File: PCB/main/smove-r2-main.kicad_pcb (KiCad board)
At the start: 4 copper layers, 25 x 30 mm, 47 parts, among them J1 TYPE-C-31-M-12, J2 Battery wire pads 2.54mm, SW2 RESET, SW3 BOOT / USER, U1 ESP32-C3-MINI-1-N4, U2 ICM-20948, U3 PCA9306DCUR, U4 AP2112K-3.3TRG1, U5 AP2112K-1.8TRG1, U6 BQ24074RGTR, U8 USBLC6-2SC6, U9 PESD5V0S2BT,215

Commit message: Make sure it's printer friendly
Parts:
- C3: value 22uF / 10V -> 22uF / 25V

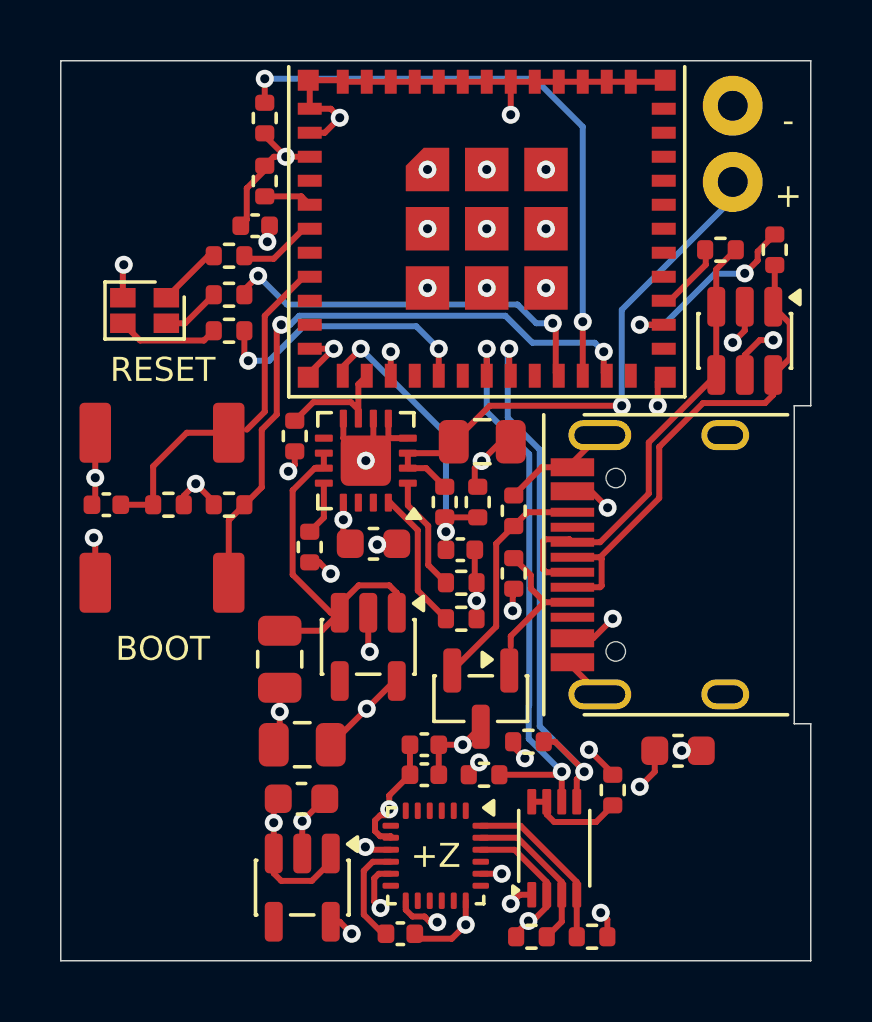
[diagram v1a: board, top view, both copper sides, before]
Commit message: Add mounting holes
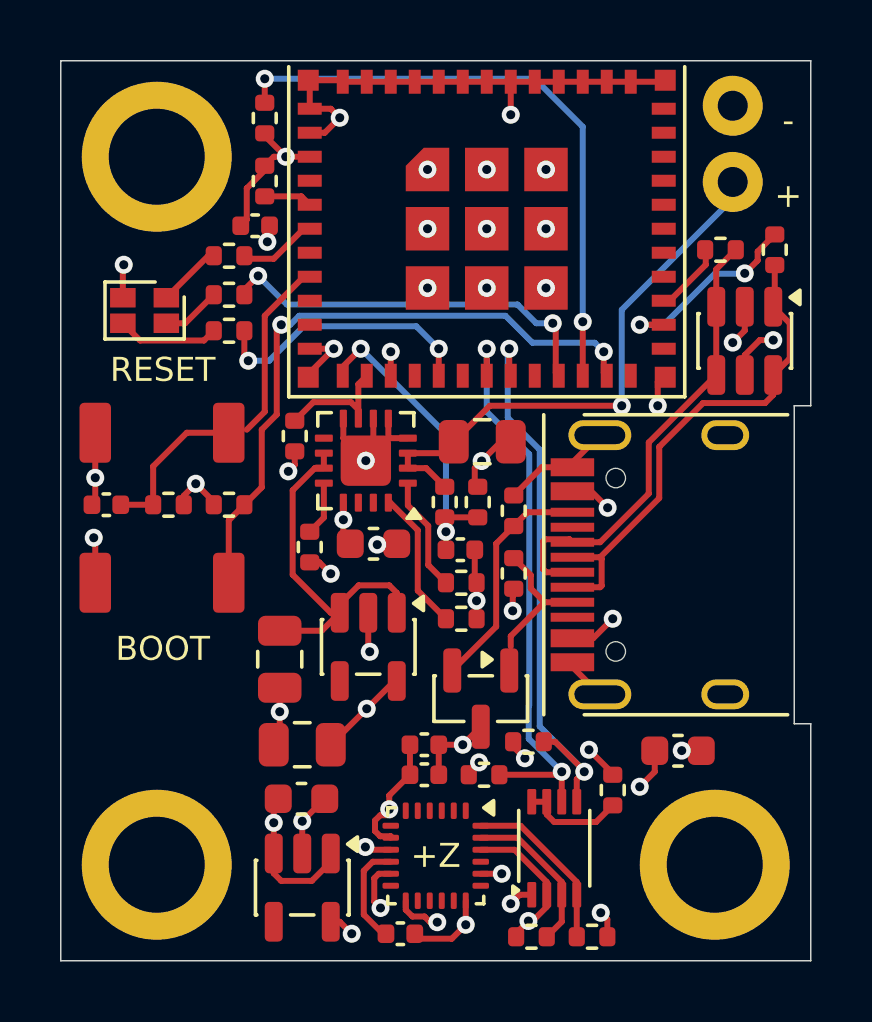
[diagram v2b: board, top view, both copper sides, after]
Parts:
- added H1: MountingHole_3.2mm_M3_Pad_5mm, smove-r2-main:MountingHole_3.2mm_M3_Pad_5mm, F.Cu at (103.2, 103.2)
- added H2: MountingHole_3.2mm_M3_Pad_5mm, smove-r2-main:MountingHole_3.2mm_M3_Pad_5mm, F.Cu at (103.2, 126.8)
- added H3: MountingHole_3.2mm_M3_Pad_5mm, smove-r2-main:MountingHole_3.2mm_M3_Pad_5mm, F.Cu at (121.8, 126.8)

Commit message: Implement routing changes
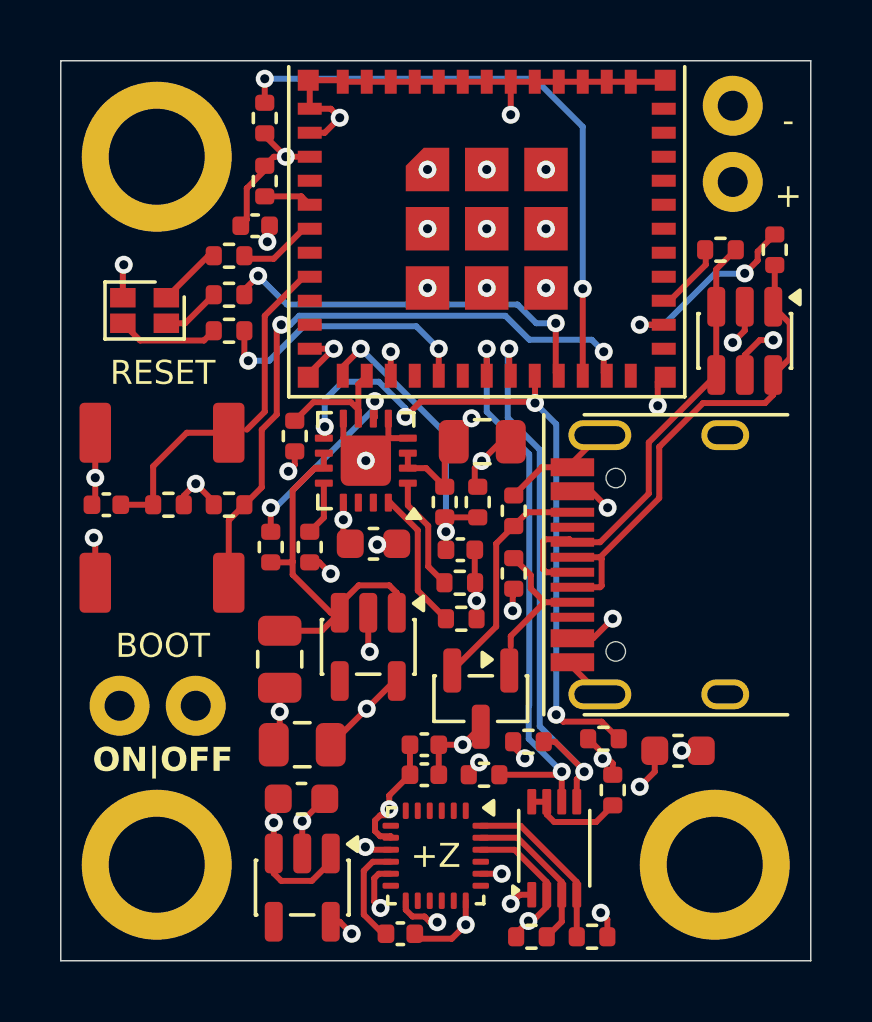
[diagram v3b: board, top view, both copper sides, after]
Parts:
- removed R23: 10k, smove-r2-main:R_0402_1005Metric
- added R24: 100k, smove-r2-main:R_0402_1005Metric, F.Cu at (118.1, 122.6)
- added R25: 100k, smove-r2-main:R_0402_1005Metric, F.Cu at (107.0, 116.2)
- added SW1: Off-board pack toggle switch (2x wire pads 2.54mm), smove-r2-main:BatteryWire_2x_PTH_P2.54mm_D1.0mm, F.Cu at (103.2, 121.5)
- added TH1: 10k B3435 NTC (cell-bonded), smove-r2-main:NTC_0402_1005Metric, F.Cu at (113.3, 117.4)
- J2: value Battery wire pads 2.54mm -> Battery wire pads 2x 2.54mm
- U4: value AP2112K-3.3TRG1 -> XC6220B331MR-G
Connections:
- J2 pad 1: /Power/PACK_P -> /Power/PACK_RAW
- U1 pad 20: unconnected-(U1-GPIO6-Pad20) -> /CHG_N
- U6 pad 1: /Power/TS_NO_CELL_SENSING -> /Power/TS
- U6 pad 6: GND -> Net-(U6-EN1)
- U6 pad 9: unconnected-(U6-CHG_N-Pad9) -> /CHG_N
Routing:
- net /Power/PACK_RAW: track 0.00 -> 27.0 mm
- net /CHG_N: track 0.00 -> 23.6 mm, vias 0 -> 4
- net /3V3_MAIN: track 63.5 -> 70.2 mm
- net Net-(U6-EN1): track 0.00 -> 6.49 mm, vias 0 -> 2
- net /Power/TS_NO_CELL_SENSING: track 3.85 -> 0.00 mm
- net /Power/TS: track 0.00 -> 3.83 mm
- net /Power/PACK_P: track 18.3 -> 21.2 mm
- net GND: track 59.7 -> 58.0 mm
- net /Power/SYS: track 12.2 -> 12.9 mm
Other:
- outline, holes or cut-outs redrawn
- board text added: "ON|OFF"

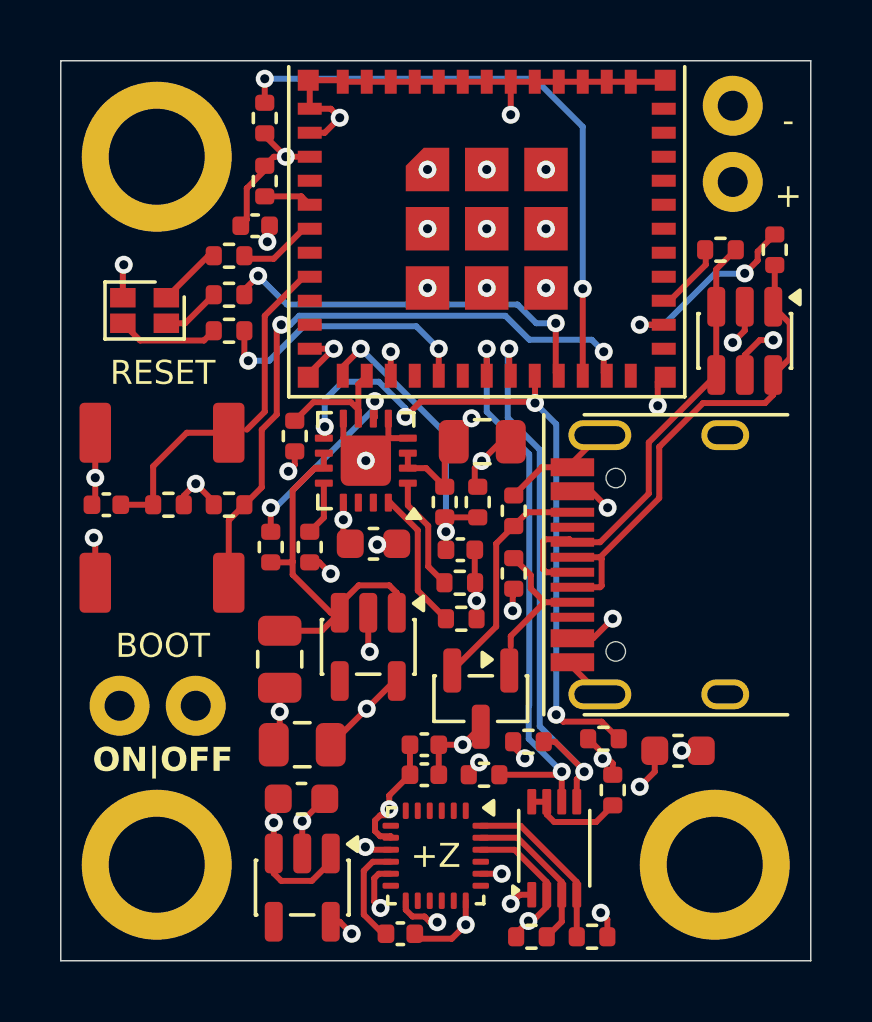
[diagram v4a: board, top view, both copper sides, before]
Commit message: board: user routing + direct C11 ground path (thermal-ECO baseline)
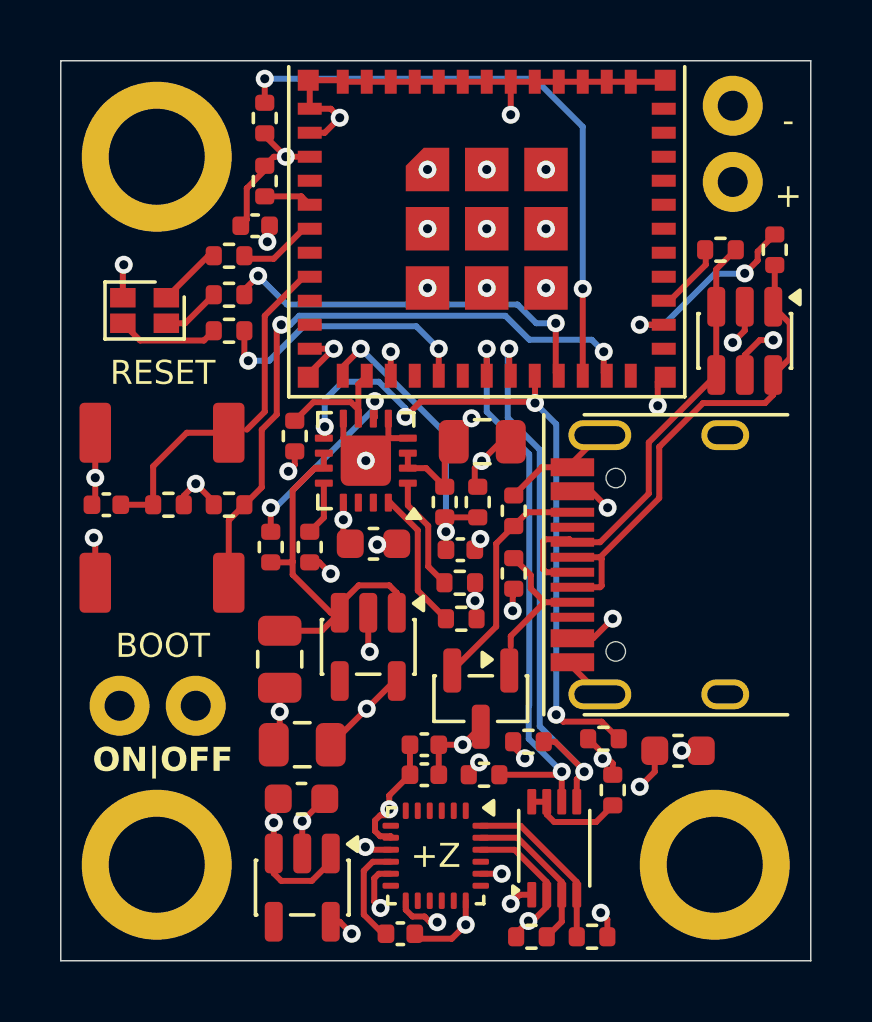
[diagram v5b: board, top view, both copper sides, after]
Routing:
- net GND: track 58.0 -> 57.4 mm, vias 34 -> 35
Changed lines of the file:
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@@
 			)
 		)
-(property "Manufacturer" "Torex Semicon"
+		(property "Manufacturer" "Torex Semicon"
 			(at 0 0 270)
 			(unlocked yes)
@@
 			)
 		)
-(property "Manufacturer" "XUNPU"
+		(property "Manufacturer" "XUNPU"
 			(at 0 0 180)
 			(unlocked yes)
@@
 			)
 		)
-(property "Manufacturer" "UNI-ROYAL(Uniroyal Elec)"
+		(property "Manufacturer" "UNI-ROYAL(Uniroyal Elec)"
 			(at 0 0 270)
 			(unlocked yes)
@@
 			)
 		)
-(property "Manufacturer" "Samsung Electro-Mechanics"
+		(property "Manufacturer" "Samsung Electro-Mechanics"
 			(at 0 0 180)
 			(unlocked yes)
@@
 			)
 		)
-(property "Manufacturer" "Samsung Electro-Mechanics"
+		(property "Manufacturer" "Samsung Electro-Mechanics"
 			(at 0 0 0)
 			(unlocked yes)
@@
 			)
 		)
-(property "Manufacturer" "XUNPU"
+		(property "Manufacturer" "XUNPU"
 			(at 0 0 180)
 			(unlocked yes)
@@
 			)
 		)
-(property "Manufacturer" "Korean Hroparts Elec"
+		(property "Manufacturer" "Korean Hroparts Elec"
 			(at 0 0 90)
 			(layer "F.SilkS")
@@
 			)
 		)
-(property "Manufacturer" "UNI-ROYAL(Uniroyal Elec)"
+		(property "Manufacturer" "UNI-ROYAL(Uniroyal Elec)"
 			(at 0 0 90)
 			(unlocked yes)
@@
 			)
 		)
-(property "Manufacturer" "STMicroelectronics"
+		(property "Manufacturer" "STMicroelectronics"
 			(at 0 0 270)
 			(unlocked yes)
@@
 			)
 		)
-(property "Manufacturer" "UNI-ROYAL(Uniroyal Elec)"
+		(property "Manufacturer" "UNI-ROYAL(Uniroyal Elec)"
 			(at 0 0 90)
 			(unlocked yes)
@@
 			)
 		)
-(property "Manufacturer" "UNI-ROYAL(Uniroyal Elec)"
+		(property "Manufacturer" "UNI-ROYAL(Uniroyal Elec)"
 			(at 0 0 270)
 			(unlocked yes)
@@
 			)
 		)
-(property "Manufacturer" "Samsung Electro-Mechanics"
+		(property "Manufacturer" "Samsung Electro-Mechanics"
 			(at 0 0 0)
 			(unlocked yes)
@@
 			)
 		)
-(property "Manufacturer" "Samsung Electro-Mechanics"
+		(property "Manufacturer" "Samsung Electro-Mechanics"
 			(at 0 0 180)
 			(unlocked yes)
@@
 			)
 		)
-(property "Manufacturer" "Espressif Systems"
+		(property "Manufacturer" "Espressif Systems"
 			(at 0 0 0)
 			(layer "F.SilkS")
@@
 			)
 		)
-(property "Manufacturer" "Nexperia"
+		(property "Manufacturer" "Nexperia"
 			(at 0 0 270)
 			(unlocked yes)
@@
 			)
 		)
-(property "Manufacturer" "Samsung Electro-Mechanics"
+		(property "Manufacturer" "Samsung Electro-Mechanics"
 			(at 0 0 0)
 			(unlocked yes)
@@
 			)
 		)
-(property "Manufacturer" "UNI-ROYAL(Uniroyal Elec)"
+		(property "Manufacturer" "UNI-ROYAL(Uniroyal Elec)"
 			(at 0 0 180)
 			(unlocked yes)
@@
 			)
 		)
-(property "Manufacturer" "Samsung Electro-Mechanics"
+		(property "Manufacturer" "Samsung Electro-Mechanics"
 			(at 0 0 270)
 			(unlocked yes)
@@
 			)
 		)
-(property "Manufacturer" "TDK"
+		(property "Manufacturer" "TDK"
 			(at 0 0 0)
 			(unlocked yes)
@@
 			)
 		)
-(property "Manufacturer" "UNI-ROYAL(Uniroyal Elec)"
+		(property "Manufacturer" "UNI-ROYAL(Uniroyal Elec)"
 			(at 0 0 270)
 			(unlocked yes)
@@
 			)
 		)
-(property "Manufacturer" "UNI-ROYAL(Uniroyal Elec)"
+		(property "Manufacturer" "UNI-ROYAL(Uniroyal Elec)"
 			(at 0 0 90)
 			(unlocked yes)
@@
 			)
 		)
-(property "Manufacturer" "UNI-ROYAL(Uniroyal Elec)"
+		(property "Manufacturer" "UNI-ROYAL(Uniroyal Elec)"
 			(at 0 0 180)
 			(unlocked yes)
@@
 			)
 		)
-(property "Manufacturer" "UNI-ROYAL(Uniroyal Elec)"
+		(property "Manufacturer" "UNI-ROYAL(Uniroyal Elec)"
 			(at 0 0 0)
 			(unlocked yes)
@@
 			)
 		)
-(property "Manufacturer" "Lite-On"
+		(property "Manufacturer" "Lite-On"
 			(at 0 0 270)
 			(unlocked yes)
@@
 			)
 		)
-(property "Manufacturer" "UNI-ROYAL(Uniroyal Elec)"
+		(property "Manufacturer" "UNI-ROYAL(Uniroyal Elec)"
 			(at 0 0 270)
 			(unlocked yes)
@@
 			)
 		)
-(property "Manufacturer" "UNI-ROYAL(Uniroyal Elec)"
+		(property "Manufacturer" "UNI-ROYAL(Uniroyal Elec)"
 			(at 0 0 180)
 			(unlocked yes)
@@
 			)
 		)
-(property "Manufacturer" "UNI-ROYAL(Uniroyal Elec)"
+		(property "Manufacturer" "UNI-ROYAL(Uniroyal Elec)"
 			(at 0 0 90)
 			(unlocked yes)
@@
 			)
 		)
-(property "Manufacturer" "UNI-ROYAL(Uniroyal Elec)"
+		(property "Manufacturer" "UNI-ROYAL(Uniroyal Elec)"
 			(at 0 0 180)
 			(unlocked yes)
@@
 			)
 		)
-(property "Manufacturer" "UNI-ROYAL(Uniroyal Elec)"
+		(property "Manufacturer" "UNI-ROYAL(Uniroyal Elec)"
 			(at 0 0 270)
 			(unlocked yes)
@@
 			)
 		)
-(property "Manufacturer" "UNI-ROYAL(Uniroyal Elec)"
+		(property "Manufacturer" "UNI-ROYAL(Uniroyal Elec)"
 			(at 0 0 90)
 			(unlocked yes)
@@
 			)
 		)
-(property "Manufacturer" "Texas Instruments"
+		(property "Manufacturer" "Texas Instruments"
 			(at 0 0 180)
 			(unlocked yes)
@@
 			)
 		)
-(property "Manufacturer" "Samsung Electro-Mechanics"
+		(property "Manufacturer" "Samsung Electro-Mechanics"
 			(at 0 0 0)
 			(unlocked yes)
@@
 			)
 		)
-(property "Manufacturer" "UNI-ROYAL(Uniroyal Elec)"
+		(property "Manufacturer" "UNI-ROYAL(Uniroyal Elec)"
 			(at 0 0 0)
 			(unlocked yes)
@@
 			)
 		)
-(property "Manufacturer" "UNI-ROYAL(Uniroyal Elec)"
+		(property "Manufacturer" "UNI-ROYAL(Uniroyal Elec)"
 			(at 0 0 0)
 			(unlocked yes)
@@
 			)
 		)
-(property "Manufacturer" "UNI-ROYAL(Uniroyal Elec)"
+		(property "Manufacturer" "UNI-ROYAL(Uniroyal Elec)"
 			(at 0 0 180)
 			(unlocked yes)
@@
 	)
 	(segment
-		(start 113.8 117.94)
-		(end 113.86 118)
-		(width 0.2)
-		(layer "F.Cu")
-		(net 18)
-	)
-	(segment
 		(start 108.25 110.45)
 		(end 109.1 109.6)
@@
 	)
 	(segment
+		(start 113.81 117.4)
+		(end 113.81 118)
+		(width 0.2)
+		(layer "F.Cu")
+		(net 18)
+	)
+	(segment
 		(start 113.035126 129.264874)
 		(end 113.5 128.8)
@@
 	)
 	(segment
-		(start 111.57 112.58)
-		(end 110.92 112.58)
+		(start 113.8 116.127486)
+		(end 113.987486 115.94)
 		(width 0.2)
 		(layer "F.Cu")
@@
 	)
 	(segment
-		(start 113.86 118)
-		(end 113.86 118.6)
+		(start 111.57 112.58)
+		(end 110.92 112.58)
 		(width 0.2)
 		(layer "F.Cu")
@@
 	)
 	(segment
-		(start 113.8 116.3)
-		(end 113.8 117.94)
-		(width 0.2)
-		(layer "F.Cu")
-		(net 18)
-	)
-	(segment
 		(start 108.25 100.65)
 		(end 109.35 100.65)
@@
 	)
 	(segment
+		(start 113.81 118)
+		(end 113.81 118.55)
+		(width 0.2)
+		(layer "F.Cu")
+		(net 18)
+	)
+	(segment
+		(start 113.81 118.55)
+		(end 113.86 118.6)
+		(width 0.2)
+		(layer "F.Cu")
+		(net 18)
+	)
+	(segment
 		(start 114.030275 113.34311)
 		(end 113.8 113.573385)
@@
 	)
 	(segment
+		(start 113.8 116.3)
+		(end 113.8 116.127486)
+		(width 0.2)
+		(layer "F.Cu")
+		(net 18)
+	)
+	(segment
 		(start 111.8 129.1)
 		(end 111.964874 129.264874)
@@
 	)
 	(via
-		(at 107.3 121.7)
+		(at 113.987486 115.94)
 		(size 0.6)
 		(drill 0.3)
@@
 	)
 	(via
-		(at 114.2 105.6)
+		(at 107.3 121.7)
 		(size 0.6)
 		(drill 0.3)
@@
 	)
 	(via
-		(at 110.658909 128.241091)
+		(at 114.2 105.6)
 		(size 0.6)
 		(drill 0.3)
@@
 	)
 	(via
-		(at 113.86 118)
+		(at 110.658909 128.241091)
 		(size 0.6)
 		(drill 0.3)
@@
 		(size 0.6)
 		(drill 0.3)
+		(layers "F.Cu" "B.Cu")
+		(net 18)
+	)
+	(via
+		(at 113.81 118)
+		(size 0.6)
+		(drill 0.3)
